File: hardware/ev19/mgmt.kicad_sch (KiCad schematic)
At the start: 24 parts, among them Q1 2N7002, Q3 2N7002, SW2 SW_Push, SW3 SW_Push, U3 STM32F072CBTx, Y1 16MHz

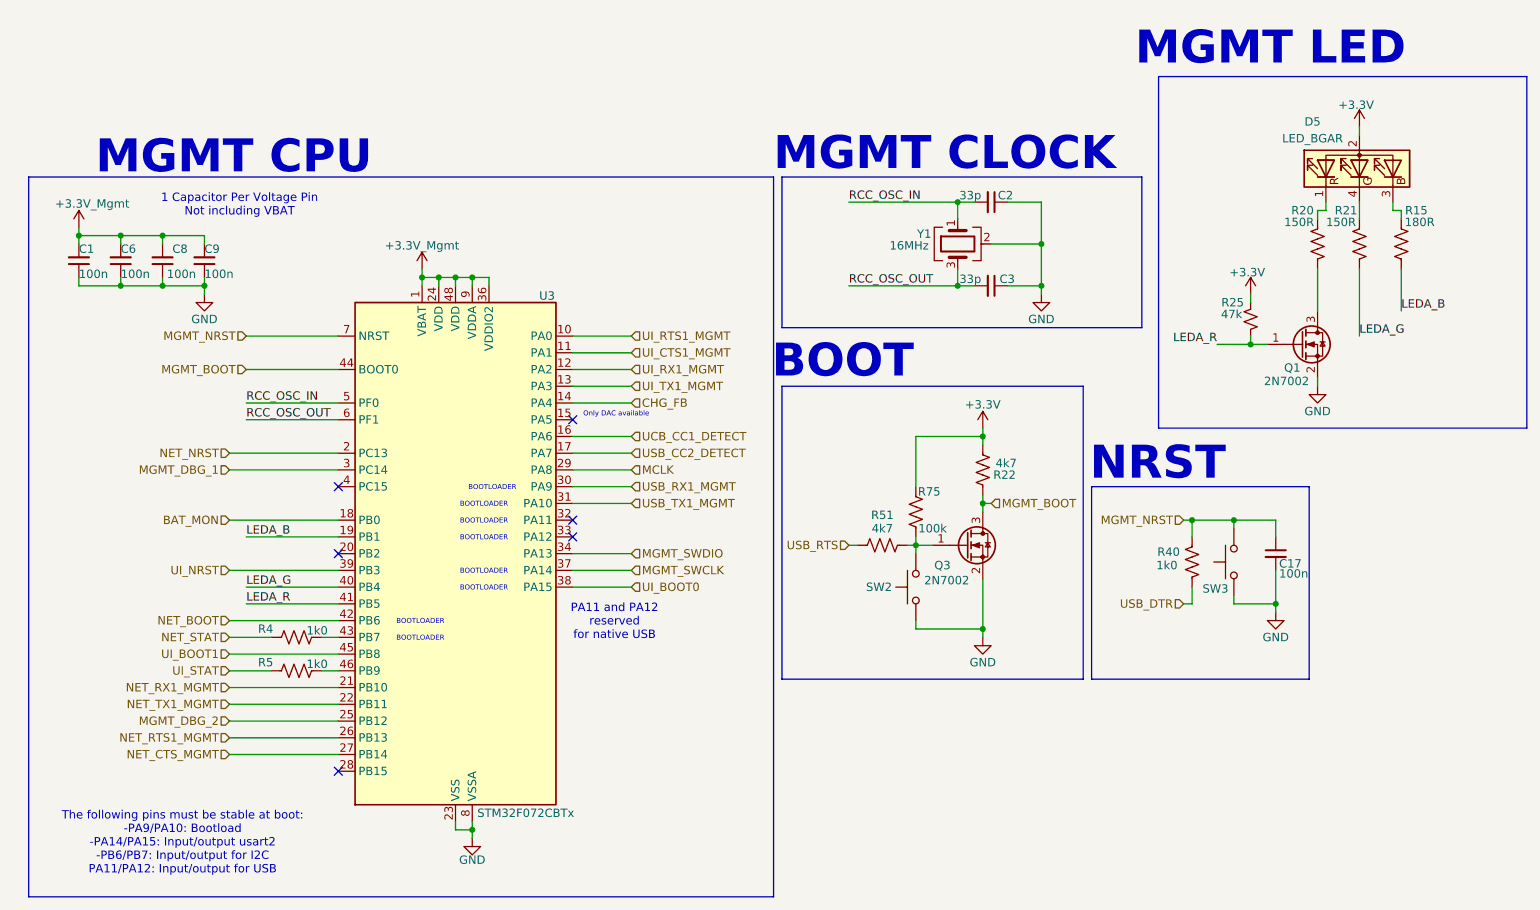
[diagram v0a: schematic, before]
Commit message: Added a sheet for the dev board and wired up the remaining connections
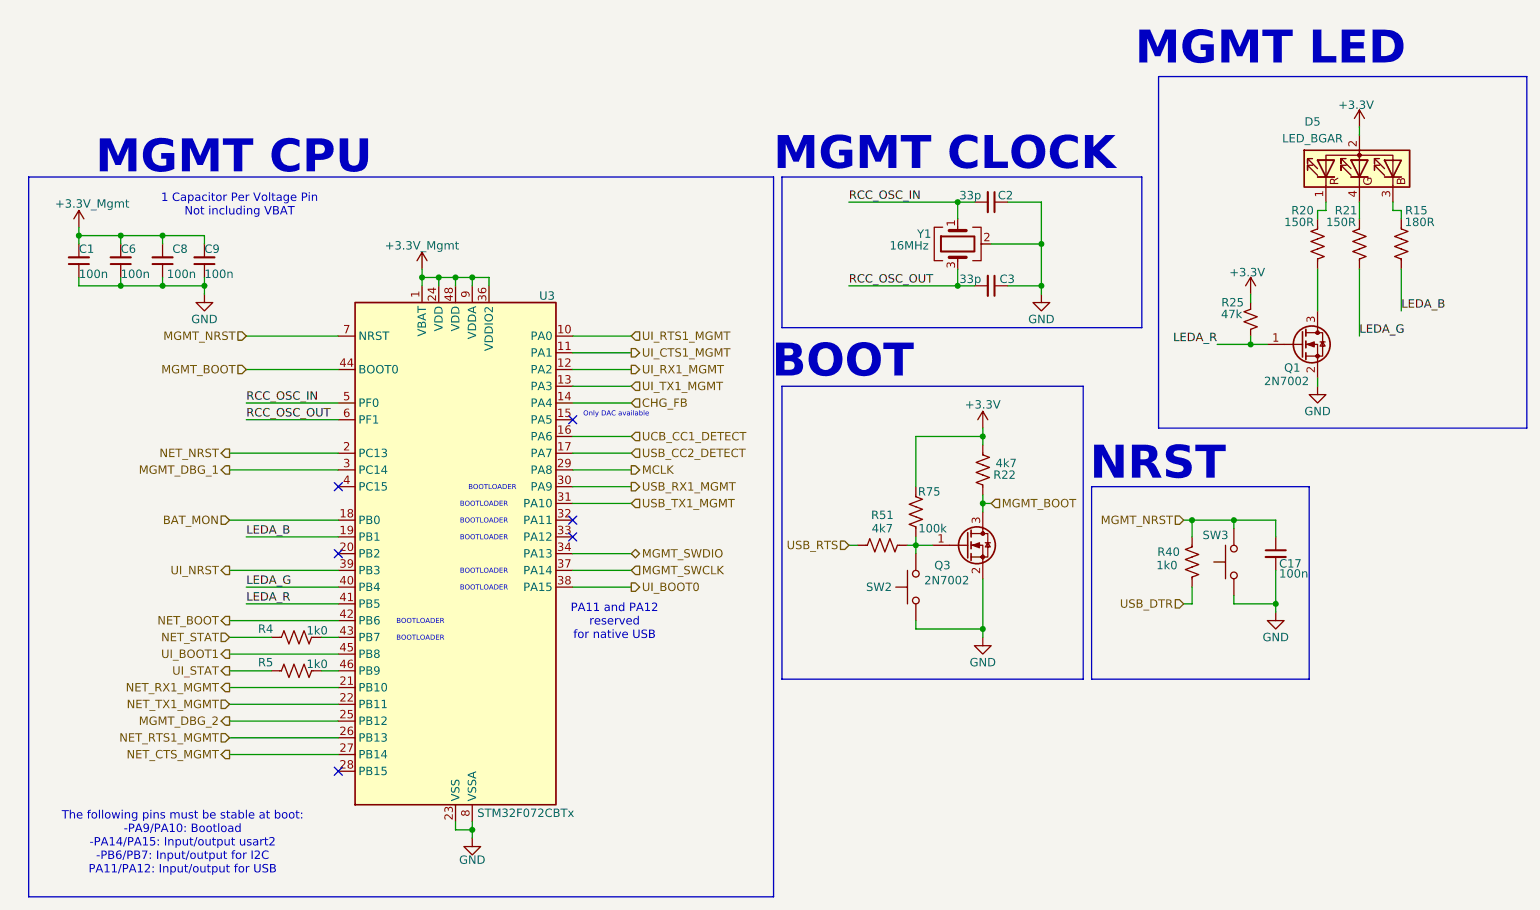
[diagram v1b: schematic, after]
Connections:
- net GND: now also SW3.3, SW3.4; no longer SW3.1, SW3.2
- net MGMT_NRST: now also SW3.1, SW3.2; no longer SW3.3, SW3.4
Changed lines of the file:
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@@
 	)
 	(hierarchical_label "UI_RX1_MGMT"
-		(shape input)
+		(shape output)
 		(at 110.49 67.31 0)
 		(effects
@@
 	)
 	(hierarchical_label "UI_NRST"
-		(shape input)
+		(shape output)
 		(at 49.53 97.79 180)
 		(effects
@@
 	)
 	(hierarchical_label "NET_CTS_MGMT"
-		(shape input)
+		(shape output)
 		(at 49.53 125.73 180)
 		(effects
@@
 	)
 	(hierarchical_label "UI_CTS1_MGMT"
-		(shape input)
+		(shape output)
 		(at 110.49 64.77 0)
 		(effects
@@
 	)
 	(hierarchical_label "USB_RX1_MGMT"
-		(shape input)
+		(shape output)
 		(at 110.49 85.09 0)
 		(effects
@@
 	)
 	(hierarchical_label "MGMT_DBG_2"
-		(shape input)
+		(shape output)
 		(at 49.53 120.65 180)
 		(effects
@@
 	)
 	(hierarchical_label "UI_STAT"
-		(shape input)
+		(shape output)
 		(at 49.53 113.03 180)
 		(effects
@@
 	)
 	(hierarchical_label "MGMT_SWDIO"
-		(shape input)
+		(shape bidirectional)
 		(at 110.49 95.25 0)
 		(effects
@@
 	)
 	(hierarchical_label "NET_BOOT"
-		(shape input)
+		(shape output)
 		(at 49.53 105.41 180)
 		(effects
@@
 	)
 	(hierarchical_label "UI_BOOT1"
-		(shape input)
+		(shape output)
 		(at 49.53 110.49 180)
 		(effects
@@
 	)
 	(hierarchical_label "UI_BOOT0"
-		(shape input)
+		(shape output)
 		(at 110.49 100.33 0)
 		(effects
@@
 	)
 	(hierarchical_label "MCLK"
-		(shape input)
+		(shape output)
 		(at 110.49 82.55 0)
 		(effects
@@
 	)
 	(hierarchical_label "NET_NRST"
-		(shape input)
+		(shape output)
 		(at 49.53 80.01 180)
 		(effects
@@
 	)
 	(hierarchical_label "NET_RX1_MGMT"
-		(shape input)
+		(shape output)
 		(at 49.53 115.57 180)
 		(effects
@@
 	)
 	(hierarchical_label "MGMT_DBG_1"
-		(shape input)
+		(shape output)
 		(at 49.53 82.55 180)
 		(effects
@@
 		(lib_id "Hactar_Symbols:SW4_Push")
 		(at 201.93 96.52 90)
+		(mirror x)
 		(unit 1)
 		(body_style 1)
@@
 		(dnp no)
 		(property "Reference" "SW3"
-			(at 199.136 100.584 90)
-			(show_name no)
-			(do_not_autoplace no)
+			(at 199.136 92.456 90)
+			(show_name no)
+			(do_not_autoplace no)
